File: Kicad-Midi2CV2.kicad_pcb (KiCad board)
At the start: 2 copper layers, 100 x 100 mm, 121 parts, among them IC101 MCP4725module, IC102 MCP4725module, J101 Doepfer connector, J102 Vin 7-12v, J103 MIDI OUT, J104 Power Conn, J105 CV7 in, J106 Gate1, J107 MIDI IN, J108 CV6 in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

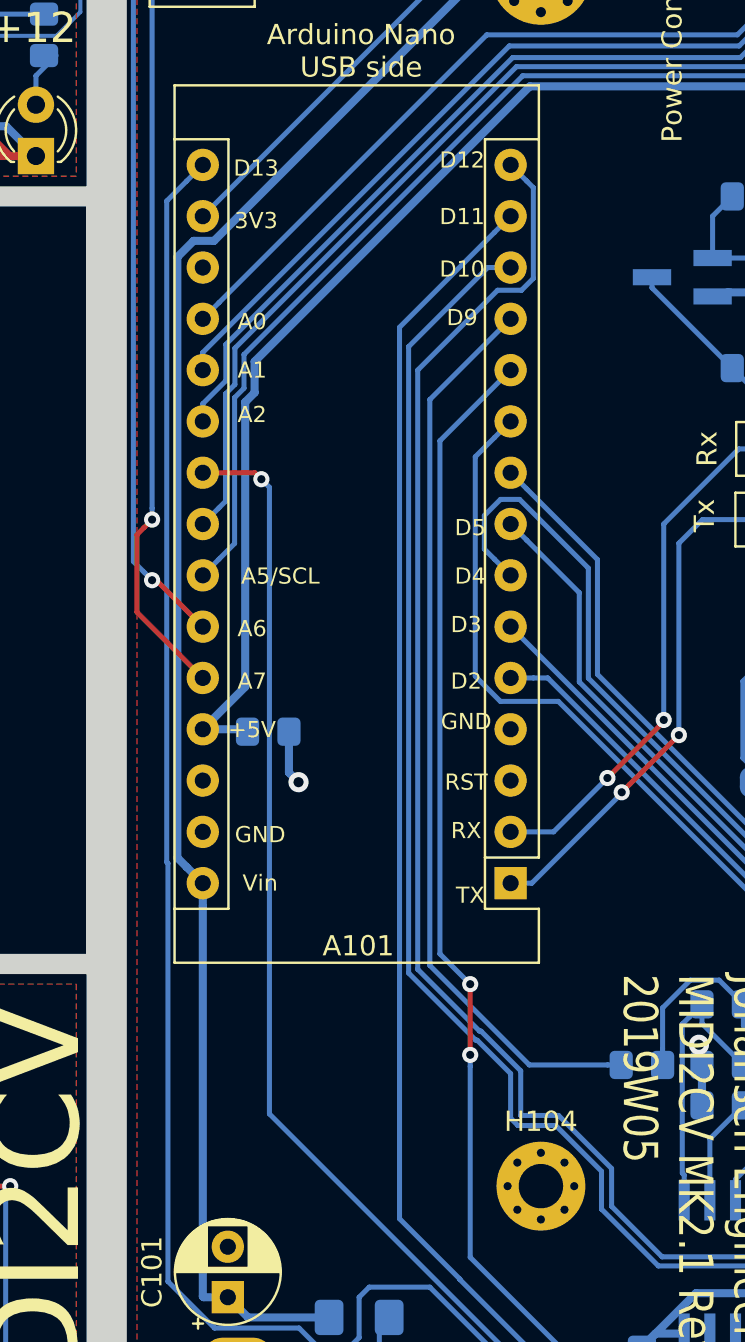
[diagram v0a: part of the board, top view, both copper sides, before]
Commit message: pinout changed in PCB
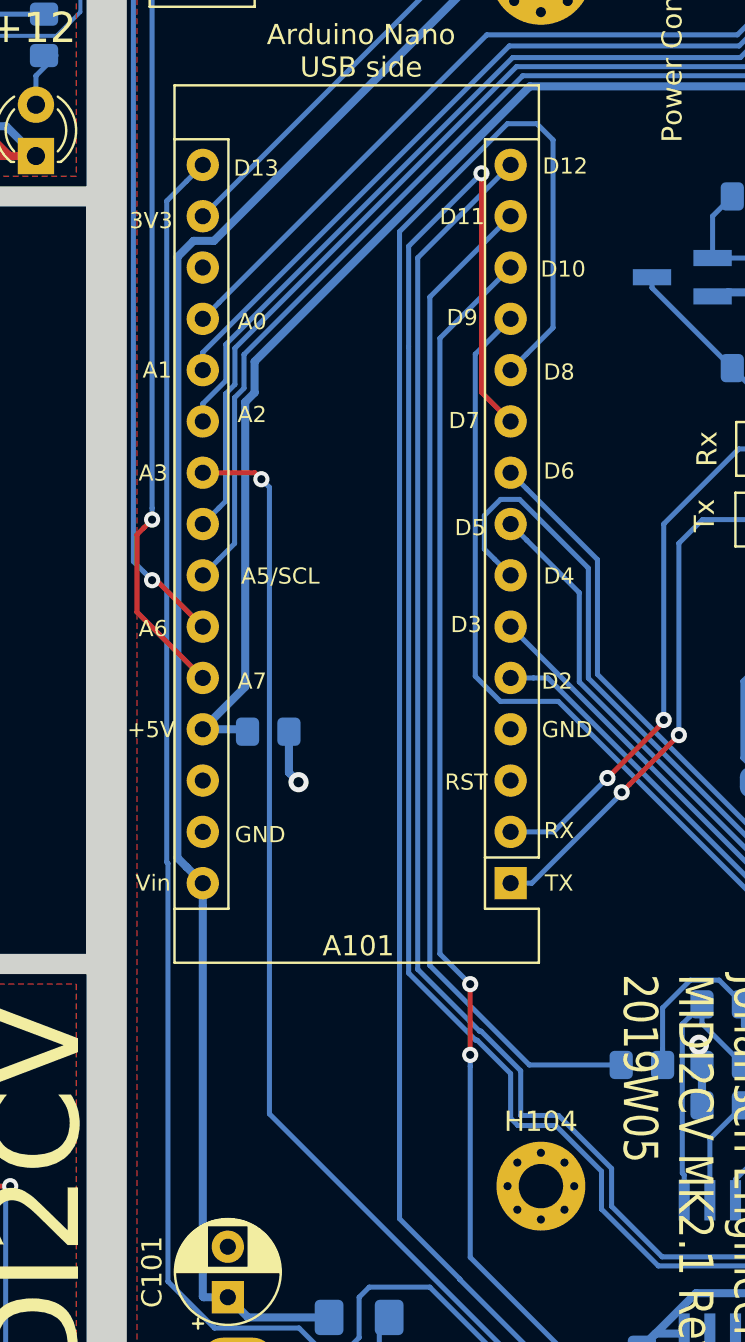
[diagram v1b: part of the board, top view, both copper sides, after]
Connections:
- A101 pad 10: Gate2 -> LED-MIDI
- A101 pad 11: Gate3 -> LED-CV1
- A101 pad 12: Gate4 -> Gate2
- A101 pad 13: LED-MIDI -> Gate3
- A101 pad 14: LED-CV1 -> Gate4
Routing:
- net LED-CV1: track 119.4 -> 138.8 mm
- net LED-MIDI: track 104.9 -> 121.1 mm, vias 0 -> 1
- net Gate4: track 45.2 -> 50.3 mm
- net Gate3: track 62.2 -> 67.3 mm
- net Gate2: track 128.3 -> 133.4 mm
- net LED-CV2: track 182.1 -> 180.4 mm
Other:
- board text added: "A3"
- board text added: "D6"
- board text added: "D7"
- board text added: "D8"

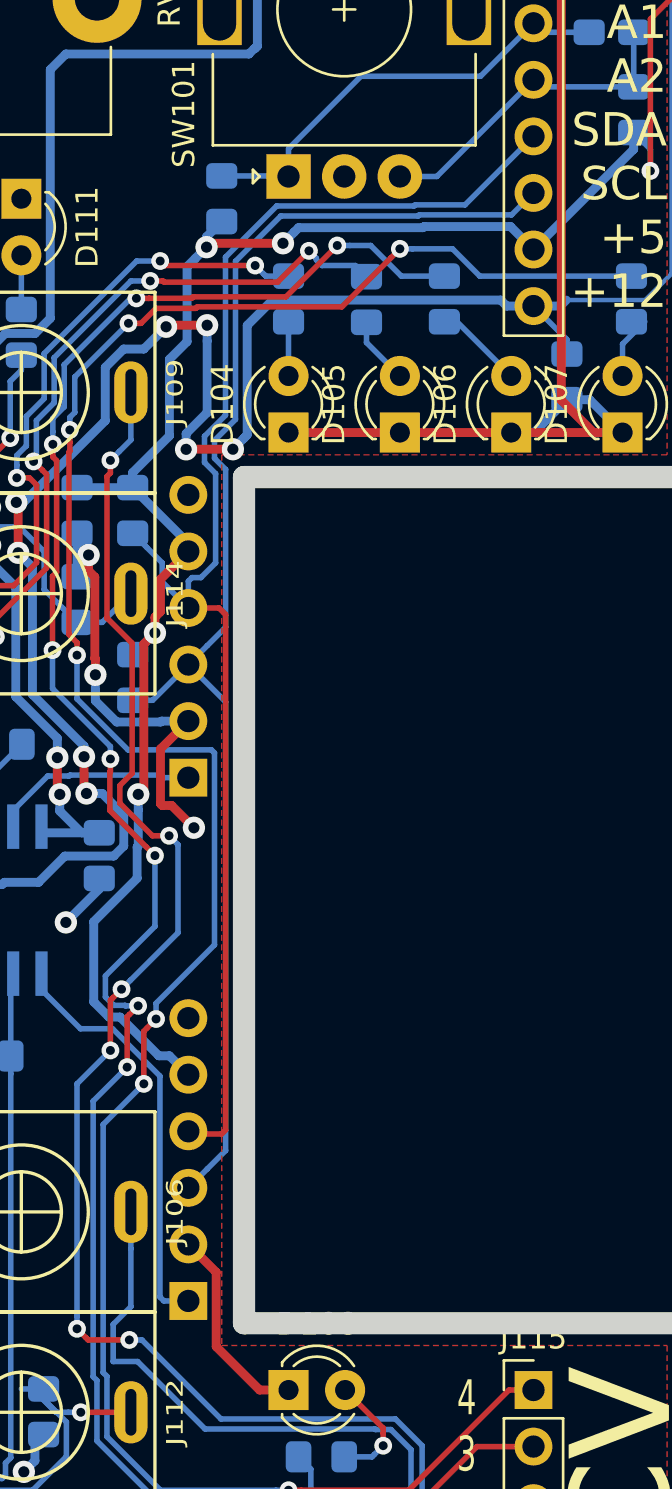
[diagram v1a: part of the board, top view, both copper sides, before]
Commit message: modify wiring - make new gerber
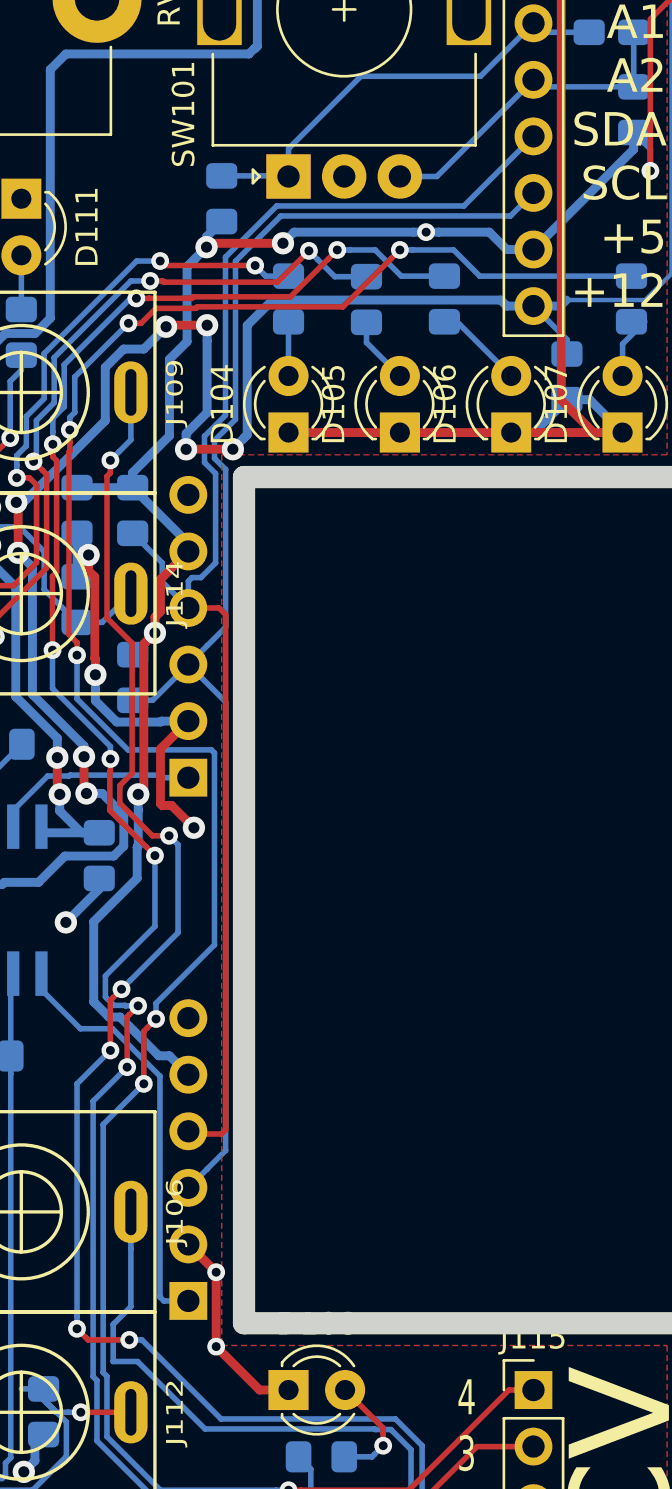
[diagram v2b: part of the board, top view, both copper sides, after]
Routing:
- net +5V: track 288.6 -> 288.4 mm, vias 10 -> 11
- net GND: vias 15 -> 17
